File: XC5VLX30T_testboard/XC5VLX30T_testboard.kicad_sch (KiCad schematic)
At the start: 28 parts, among them J1 Conn_01x35_Pin, J10 Conn_01x04_Pin, J11 Conn_01x04_Pin, J12 Conn_01x04_Pin, J13 Conn_01x04_Pin, J14 Conn_01x04_Pin, J2 Conn_01x35_Pin, J3 Conn_01x35_Pin, J4 Conn_01x35_Pin, J5 Conn_01x35_Pin, J6 Conn_01x35_Pin, J7 Conn_01x35_Pin, J8 Conn_01x35_Pin, J9 Conn_01x04_Pin, U1 XC5VLX30T-1FFG665C, X1 SG-5032CCN

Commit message: mode select pins + pull down resistors
"If the Virtex-5 device is configured via JTAG on power-up, it is advisable to tie the mode pins to the Boundary-Scan configuration mode settings: 101 (M2 = 1, M1 = 0,
M0 = 1)."
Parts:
- added R1, R2, R3: R, Resistor_SMD:R_0201_0603Metric, symbol Device:R
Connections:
- net GND: now also R1.2
- net VCCO: now also R2.2, R3.2
- net M0_MODESELECT: now reaches U1.T20 (M0_0)
- net M0_MODESELECT: now also R3.1
- net M2_MODESELECT: now reaches U1.U20 (M2_0)
- net M2_MODESELECT: now also R2.1
- net M1_MODESELECT: now reaches U1.W20 (M1_0)
- net M1_MODESELECT: now also R1.1
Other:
- note removed: "top layer, 1st bottom row - AF"
- note removed: "top layer, 2nd bottom row - AE"

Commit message: resize wires to .13mm
resized wires to 0.13mm
added top layer gnd plane, vccaux plane
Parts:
- added C10, C11, C14, C16, C17: 470uF, Capacitor_Tantalum_SMD:CP_EIA-3216-12_Kemet-S, symbol Device:C
- added TP1, TP2, TP3, TP4: TestPoint, Connector_Pin:Pin_D0.7mm_L6.5mm_W1.8mm_FlatFork, symbol Connector:TestPoint
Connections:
- net GND: now also J10.3 (Pin_3), J10.4 (Pin_4), J11.1 (Pin_1), J11.2 (Pin_2), J12.3 (Pin_3), J12.4 (Pin_4), J13.1 (Pin_1), J13.2 (Pin_2), J14.3 (Pin_3), J14.4 (Pin_4), J9.1 (Pin_1), J9.2 (Pin_2), C10.2, C11.2, C14.2, C16.2, C17.2; no longer J10.1 (Pin_1), J10.2 (Pin_2), J11.3 (Pin_3), J11.4 (Pin_4), J12.1 (Pin_1), J12.2 (Pin_2), J13.3 (Pin_3), J13.4 (Pin_4), J14.1 (Pin_1), J14.2 (Pin_2), J9.3 (Pin_3), J9.4 (Pin_4)
- net IO_L8N_CC_SM1N_13: now also J6.30 (Pin_30); no longer J6.32 (Pin_32)
- net IO_L8P_CC_SM1P_13: now also J6.32 (Pin_32); no longer J6.31 (Pin_31)
- net IO_L9P_CC_SM0P_13: now also J6.31 (Pin_31); no longer J6.30 (Pin_30)
- net TCK: now also TP2.1
- net TDI: now also TP3.1
- net TDO: now also TP1.1
- net TMS: now also TP4.1
- net VCCO: now also J12.1 (Pin_1), J12.2 (Pin_2), C10.1, C11.1; no longer J12.3 (Pin_3), J12.4 (Pin_4)
- net VccAUX: now also J10.1 (Pin_1), J10.2 (Pin_2); no longer J10.3 (Pin_3), J10.4 (Pin_4)
- net VccINT: now also J14.1 (Pin_1), J14.2 (Pin_2); no longer J14.3 (Pin_3), J14.4 (Pin_4)
- net vccext: now also J11.3 (Pin_3), J11.4 (Pin_4), J13.3 (Pin_3), J13.4 (Pin_4), J9.3 (Pin_3), J9.4 (Pin_4), C14.1, C16.1, C17.1; no longer J11.1 (Pin_1), J11.2 (Pin_2), J13.1 (Pin_1), J13.2 (Pin_2), J9.1 (Pin_1), J9.2 (Pin_2)

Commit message: moved clock to P from N
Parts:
- added TP5: TestPoint, Connector_Pin:Pin_D0.7mm_L6.5mm_W1.8mm_FlatFork, symbol Connector:TestPoint
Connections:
- net CLK: now also U1.AC17 (IO_L8P_CC_GC_4); no longer U1.AC16 (IO_L9N_CC_GC_4)
- net GND: no longer J11.2 (Pin_2), J13.2 (Pin_2), J9.2 (Pin_2)
- net IO_L8P_CC_GC_4: now also U1.AC16 (IO_L9N_CC_GC_4); no longer U1.AC17 (IO_L8P_CC_GC_4)
- net vccext: no longer J11.3 (Pin_3), J13.3 (Pin_3), J9.3 (Pin_3)
- net CLK_AUX1: now reaches U1.D16 (IO_L1P_CC_GC_3)
- net CLK_AUX1: now also TP5.1
- no-connect marks 24 -> 188
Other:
- note added: "FPGA"
- note added: "VCCO capacitors"
- note added: "active crystal osc"
- note added: "jtag pins bottom side"
- note added: "power converters"
- note added: "vccaux capacitors"
- note added: "vccext capacitors"
- moved on the sheet: C1, C10, C11, C12, C13, C14, C15, C16, C17, C2, C3, C4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

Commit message: added jtag header and pi zero footprint
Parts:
- removed J10, J11, J12, J13, J14, J9: Conn_01x04_Pin, Connector_PinHeader_2.54mm:PinHeader_1x04_P2.54mm_Vertical, symbol Connector:Conn_01x04_Pin
- added J10: pi_zero_footprint_placeholder, pizero_23x58_mountholes:23x58pizero, symbol Connector_Generic:Conn_02x03_Counter_Clockwise
- added J11: Conn_01x02_Pin, Connector_PinSocket_2.54mm:PinSocket_1x02_P2.54mm_Vertical, symbol Connector:Conn_01x02_Pin
- added J15, J16, J17: Conn_01x06_Pin, virtex5_buck_footprint:virtex5_buck, symbol Connector:Conn_01x06_Pin
- added J9: Conn_02x03, Connector_PinHeader_2.54mm:PinHeader_2x03_P2.54mm_Vertical, symbol Connector_Generic:Conn_02x03_Counter_Clockwise
- added TP6, TP7, TP8, TP9: TestPoint, Connector_Pin:Pin_D0.7mm_L6.5mm_W1.8mm_FlatFork, symbol Connector:TestPoint
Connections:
- net GND: now also J11.1 (Pin_1), J15.3 (Pin_3), J15.4 (Pin_4), J15.5 (Pin_5), J16.3 (Pin_3), J16.4 (Pin_4), J16.5 (Pin_5), J17.3 (Pin_3), J17.4 (Pin_4), J17.5 (Pin_5), J9.2 (Pin_2)
- net VCCO: now also J17.1 (Pin_1), J17.2 (Pin_2), J9.1 (Pin_1)
- net VccAUX: now also J15.1 (Pin_1), J15.2 (Pin_2)
- net VccINT: now also J16.1 (Pin_1), J16.2 (Pin_2)
- net vccext: now also J11.2 (Pin_2), J15.6 (Pin_6), J16.6 (Pin_6), J17.6 (Pin_6)
- new net TCK_PAD: J9.5 (Pin_5), TP8.1
- new net TDI_PAD: J9.4 (Pin_4), TP7.1
- new net TDO_PAD: J9.6 (Pin_6), TP9.1
- new net TMS_PAD: J9.3 (Pin_3), TP6.1
- no-connect marks 188 -> 182
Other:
- moved on the sheet: TP1, TP2, TP3, TP4, TP5

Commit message: gnd planes
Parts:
- removed J10: pi_zero_footprint_placeholder, pizero_23x58_mountholes:23x58pizero, symbol Connector_Generic:Conn_02x03_Counter_Clockwise
- added J12: pi_zero_footprint_placeholder, pizero_23x58_mountholes:23x58pizero, symbol Connector_Generic:Conn_02x03_Counter_Clockwise
- TP1, TP2, TP3, TP4, TP5, TP6, TP7, TP8, TP9: footprint Connector_Pin:Pin_D0.7mm_L6.5mm_W1.8mm_FlatFork -> virtex5_buck_footprint:thisone_TestPoint_Pad_D1.0mm
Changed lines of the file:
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@@
 	(wire
 		(pts
+			(xy 60.96 469.9) (xy 69.85 469.9)
+		)
+		(stroke
+			(width 0)
+			(type default)
+		)
+	)
+	(wire
+		(pts
 			(xy 260.35 119.38) (xy 264.16 119.38)
 		)
@@
 	(wire
 		(pts
-			(xy 214.63 497.84) (xy 226.06 497.84)
-		)
-		(stroke
-			(width 0)
-			(type default)
-		)
-	)
-	(wire
-		(pts
 			(xy 861.06 85.09) (xy 857.25 85.09)
 		)
@@
 		)
 	)
+	(global_label "CLK_AUX1"
+		(shape input)
+		(at 69.85 469.9 0)
+		(fields_autoplaced yes)
+		(effects
+			(font
+				(size 1.27 1.27)
+			)
+			(justify left)
+		)
+		(property "Intersheetrefs" "${INTERSHEET_REFS}"
+			(at 82.209 469.9 0)
+			(effects
+				(font
+					(size 1.27 1.27)
+				)
+				(justify left)
+				(hide yes)
+			)
+		)
+	)
 	(global_label "IO_L18N_13"
 		(shape input)
@@
 		)
 	)
-	(global_label "CLK_AUX1"
-		(shape input)
-		(at 226.06 497.84 0)
-		(fields_autoplaced yes)
-		(effects
-			(font
-				(size 1.27 1.27)
-			)
-			(justify left)
-		)
-		(property "Intersheetrefs" "${INTERSHEET_REFS}"
-			(at 238.419 497.84 0)
-			(effects
-				(font
-					(size 1.27 1.27)
-				)
-				(justify left)
-				(hide yes)
-			)
-		)
-	)
 	(global_label "IO_L18N_18"
 		(shape bidirectional)
@@
 			)
 		)
-		(property "Footprint" "Connector_Pin:Pin_D0.7mm_L6.5mm_W1.8mm_FlatFork"
+		(property "Footprint" "virtex5_buck_footprint:thisone_TestPoint_Pad_D1.0mm"
 			(at 72.39 449.58 0)
 			(effects
@@
 			)
 		)
-		(property "Footprint" "Connector_Pin:Pin_D0.7mm_L6.5mm_W1.8mm_FlatFork"
+		(property "Footprint" "virtex5_buck_footprint:thisone_TestPoint_Pad_D1.0mm"
 			(at 132.08 443.23 0)
 			(effects
@@
 			)
 		)
-		(property "Footprint" "Connector_Pin:Pin_D0.7mm_L6.5mm_W1.8mm_FlatFork"
+		(property "Footprint" "virtex5_buck_footprint:thisone_TestPoint_Pad_D1.0mm"
 			(at 95.25 440.69 0)
 			(effects
@@
 	)
 	(symbol
+		(lib_id "Connector_Generic:Conn_02x03_Counter_Clockwise")
+		(at 469.9 596.9 0)
+		(unit 1)
+		(exclude_from_sim no)
+		(in_bom yes)
+		(on_board yes)
+		(dnp no)
+		(fields_autoplaced yes)
+		(property "Reference" "J12"
+			(at 471.17 588.01 0)
+			(effects
+				(font
+					(size 1.27 1.27)
+				)
+			)
+		)
+		(property "Value" "pi_zero_footprint_placeholder"
+			(at 471.17 590.55 0)
+			(effects
+				(font
+					(size 1.27 1.27)
+				)
+			)
+		)
+		(property "Footprint" "pizero_23x58_mountholes:23x58pizero"
+			(at 469.9 596.9 0)
+			(effects
+				(font
+					(size 1.27 1.27)
+				)
+				(hide yes)
+			)
+		)
+		(property "Datasheet" "~"
+			(at 469.9 596.9 0)
+			(effects
+				(font
+					(size 1.27 1.27)
+				)
+				(hide yes)
+			)
+		)
+		(property "Description" "Generic connector, double row, 02x03, counter clockwise pin numbering scheme (similar to DIP package numbering), script generated (kicad-library-utils/schlib/autogen/connector/)"
+			(at 469.9 596.9 0)
+			(effects
+				(font
+					(size 1.27 1.27)
+				)
+				(hide yes)
+			)
+		)
+		(pin "3"
+		)
+		(pin "2"
+		)
+		(pin "4"
+		)
+		(pin "5"
+		)
+		(pin "6"
+		)
+		(pin "1"
+		)
+		(instances
+			(project "XC5VLX30T_testboard"
+				(path "/67cccbfc-a73c-4a35-9756-6da624b7ab36"
+					(reference "J12")
+					(unit 1)
+				)
+			)
+		)
+	)
+	(symbol
 		(lib_id "power:GND")
 		(at 40.64 125.73 270)
@@
 			)
 		)
-		(property "Footprint" "Connector_Pin:Pin_D0.7mm_L6.5mm_W1.8mm_FlatFork"
+		(property "Footprint" "virtex5_buck_footprint:thisone_TestPoint_Pad_D1.0mm"
 			(at 129.54 439.42 0)
 			(effects
@@
 			)
 		)
-		(property "Footprint" "Connector_Pin:Pin_D0.7mm_L6.5mm_W1.8mm_FlatFork"
+		(property "Footprint" "virtex5_buck_footprint:thisone_TestPoint_Pad_D1.0mm"
 			(at 69.85 444.5 0)
 			(effects
@@
 	)
 	(symbol
+		(lib_id "Connector:TestPoint")
+		(at 60.96 469.9 0)
+		(unit 1)
+		(exclude_from_sim no)
+		(in_bom yes)
+		(on_board yes)
+		(dnp no)
+		(fields_autoplaced yes)
+		(property "Reference" "TP5"
+			(at 63.5 465.3279 0)
+			(effects
+				(font
+					(size 1.27 1.27)
+				)
+				(justify left)
+			)
+		)
+		(property "Value" "TestPoint"
+			(at 63.5 467.8679 0)
+			(effects
+				(font
+					(size 1.27 1.27)
+				)
+				(justify left)
+			)
+		)
+		(property "Footprint" "virtex5_buck_footprint:thisone_TestPoint_Pad_D1.0mm"
+			(at 66.04 469.9 0)
+			(effects
+				(font
+					(size 1.27 1.27)
+				)
+				(hide yes)
+			)
+		)
+		(property "Datasheet" "~"
+			(at 66.04 469.9 0)
+			(effects
+				(font
+					(size 1.27 1.27)
+				)
+				(hide yes)
+			)
+		)
+		(property "Description" "test point"
+			(at 60.96 469.9 0)
+			(effects
+				(font
+					(size 1.27 1.27)
+				)
+				(hide yes)
+			)
+		)
+		(pin "1"
+		)
+		(instances
+			(project "XC5VLX30T_testboard"
+				(path "/67cccbfc-a73c-4a35-9756-6da624b7ab36"
+					(reference "TP5")
+					(unit 1)
+				)
+			)
+		)
+	)
+	(symbol
 		(lib_id "power:GND")
 		(at 435.61 48.26 90)
@@
 	)
 	(symbol
-		(lib_id "Connector_Generic:Conn_02x03_Counter_Clockwise")
-		(at 443.23 600.71 0)
-		(unit 1)
-		(exclude_from_sim no)
-		(in_bom yes)
-		(on_board yes)
-		(dnp no)
-		(fields_autoplaced yes)
-		(property "Reference" "J10"
-			(at 444.5 591.82 0)
-			(effects
-				(font
-					(size 1.27 1.27)
-				)
-			)
-		)
-		(property "Value" "pi_zero_footprint_placeholder"
-			(at 444.5 594.36 0)
-			(effects
-				(font
-					(size 1.27 1.27)
-				)
-			)
-		)
-		(property "Footprint" "pizero_23x58_mountholes:23x58pizero"
-			(at 443.23 600.71 0)
-			(effects
-				(font
-					(size 1.27 1.27)
-				)
-				(hide yes)
-			)
-		)
-		(property "Datasheet" "~"
-			(at 443.23 600.71 0)
-			(effects
-				(font
-					(size 1.27 1.27)
-				)
-				(hide yes)
-			)
-		)
-		(property "Description" "Generic connector, double row, 02x03, counter clockwise pin numbering scheme (similar to DIP package numbering), script generated (kicad-library-utils/schlib/autogen/connector/)"
-			(at 443.23 600.71 0)
-			(effects
-				(font
-					(size 1.27 1.27)
-				)
-				(hide yes)
-			)
-		)
-		(pin "3"
-		)
-		(pin "2"
-		)
-		(pin "4"
-		)
-		(pin "5"
-		)
-		(pin "6"
-		)
-		(pin "1"
-		)
-		(instances
-			(project "XC5VLX30T_testboard"
-				(path "/67cccbfc-a73c-4a35-9756-6da624b7ab36"
-					(reference "J10")
-					(unit 1)
-				)
-			)
-		)
-	)
-	(symbol
 		(lib_id "power:GND")
 		(at 278.13 149.86 270)
@@
 	)
 	(symbol
-		(lib_id "Connector:TestPoint")
-		(at 214.63 497.84 0)
-		(unit 1)
-		(exclude_from_sim no)
-		(in_bom yes)
-		(on_board yes)
-		(dnp no)
-		(fields_autoplaced yes)
-		(property "Reference" "TP5"
-			(at 217.17 493.2679 0)
-			(effects
-				(font
-					(size 1.27 1.27)
-				)
-				(justify left)
-			)
-		)
-		(property "Value" "TestPoint"
-			(at 217.17 495.8079 0)
-			(effects
-				(font
-					(size 1.27 1.27)
-				)
-				(justify left)
-			)
-		)
-		(property "Footprint" "Connector_Pin:Pin_D0.7mm_L6.5mm_W1.8mm_FlatFork"
-			(at 219.71 497.84 0)
-			(effects
-				(font
-					(size 1.27 1.27)
-				)
-				(hide yes)
-			)
-		)
-		(property "Datasheet" "~"
-			(at 219.71 497.84 0)
-			(effects
-				(font
-					(size 1.27 1.27)
-				)
-				(hide yes)
-			)
-		)
-		(property "Description" "test point"
-			(at 214.63 497.84 0)
-			(effects
-				(font
-					(size 1.27 1.27)
-				)
-				(hide yes)
-			)
-		)
-		(pin "1"
-		)
-		(instances
-			(project "XC5VLX30T_testboard"
-				(path "/67cccbfc-a73c-4a35-9756-6da624b7ab36"
-					(reference "TP5")
-					(unit 1)
-				)
-			)
-		)
-	)
-	(symbol
 		(lib_id "power:GND")
 		(at 176.53 271.78 90)
@@
 			)
 		)
-		(property "Footprint" "Connector_Pin:Pin_D0.7mm_L6.5mm_W1.8mm_FlatFork"
+		(property "Footprint" "virtex5_buck_footprint:thisone_TestPoint_Pad_D1.0mm"
 			(at 67.31 439.42 0)
 			(effects
@@
 			)
 		)
-		(property "Footprint" "Connector_Pin:Pin_D0.7mm_L6.5mm_W1.8mm_FlatFork"
+		(property "Footprint" "virtex5_buck_footprint:thisone_TestPoint_Pad_D1.0mm"
 			(at 76.2 455.93 0)
 			(effects
@@
 			)
 		)
-		(property "Footprint" "Connector_Pin:Pin_D0.7mm_L6.5mm_W1.8mm_FlatFork"
+		(property "Footprint" "virtex5_buck_footprint:thisone_TestPoint_Pad_D1.0mm"
 			(at 127 450.85 0)
 			(effects

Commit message: removed 4 i/o for wider vccint
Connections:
- net GND: now also J12.1 (Pin_1), J4.10 (Pin_10), J4.11 (Pin_11), J4.8 (Pin_8), J4.9 (Pin_9)
- net IO_L0P_SM8P_13: now also J6.10 (Pin_10); no longer J6.11 (Pin_11)
- net IO_L10P_CC_12: now also J1.13 (Pin_13); no longer J1.15 (Pin_15)
- net IO_L11P_CC_12: now also J1.29 (Pin_29); no longer J1.27 (Pin_27)
- net IO_L12N_VRP_15: now also J4.32 (Pin_32); no longer J4.33 (Pin_33)
- net IO_L12P_VRN_17: now also J7.5 (Pin_5); no longer J7.6 (Pin_6)
- net IO_L13N_17: now also J7.3 (Pin_3); no longer J7.4 (Pin_4)
- net IO_L13P_12: now also J1.27 (Pin_27); no longer J1.29 (Pin_29)
- net IO_L13P_17: now also J7.6 (Pin_6); no longer J7.5 (Pin_5)
- net IO_L14N_VREF_15: now also J4.33 (Pin_33); no longer J4.32 (Pin_32)
- net IO_L16P_SM12P_11: now also J6.8 (Pin_8); no longer J6.9 (Pin_9)
- net IO_L18N_SM10N_11: now also J6.11 (Pin_11); no longer J6.10 (Pin_10)
- net IO_L19N_SM9N_11: now also J6.9 (Pin_9); no longer J6.8 (Pin_8)
- net IO_L7P_12: now also J1.15 (Pin_15); no longer J1.13 (Pin_13)
- net IO_L9P_CC_17: now also J7.4 (Pin_4); no longer J7.3 (Pin_3)
- net IO_L0N_15: no longer names the net of U1.C14 (IO_L0N_15)
- net IO_L0N_15: no longer J4.9 (Pin_9)
- net IO_L0P_15: no longer names the net of U1.C13 (IO_L0P_15)
- net IO_L0P_15: no longer J4.8 (Pin_8)
- net IO_L1P_15: no longer names the net of U1.B14 (IO_L1P_15)
- net IO_L1P_15: no longer J4.11 (Pin_11)
- net IO_L2P_15: no longer names the net of U1.A14 (IO_L2P_15)
- net IO_L2P_15: no longer J4.10 (Pin_10)
- no-connect marks 182 -> 186

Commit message: w
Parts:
- X1: footprint Crystal:Crystal_SMD_3225-4Pin_3.2x2.5mm_HandSoldering -> Crystal:Crystal_SMD_7050-4Pin_7.0x5.0mm
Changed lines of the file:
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@@
 			)
 		)
-		(property "Footprint" "Crystal:Crystal_SMD_3225-4Pin_3.2x2.5mm_HandSoldering"
+		(property "Footprint" "Crystal:Crystal_SMD_7050-4Pin_7.0x5.0mm"
 			(at 88.9 525.78 0)
 			(effects
@@
 		)
 		(instances
-			(project ""
+			(project "XC5VLX30T_testboard"
 				(path "/67cccbfc-a73c-4a35-9756-6da624b7ab36"
 					(reference "J15")
@@
 		)
 		(instances
-			(project ""
+			(project "XC5VLX30T_testboard"
 				(path "/67cccbfc-a73c-4a35-9756-6da624b7ab36"
 					(reference "J9")
@@
 		)
 		(instances
-			(project ""
+			(project "XC5VLX30T_testboard"
 				(path "/67cccbfc-a73c-4a35-9756-6da624b7ab36"
 					(reference "J11")
@@
 		)
 		(instances
-			(project ""
+			(project "XC5VLX30T_testboard"
 				(path "/67cccbfc-a73c-4a35-9756-6da624b7ab36"
 					(reference "TP1")

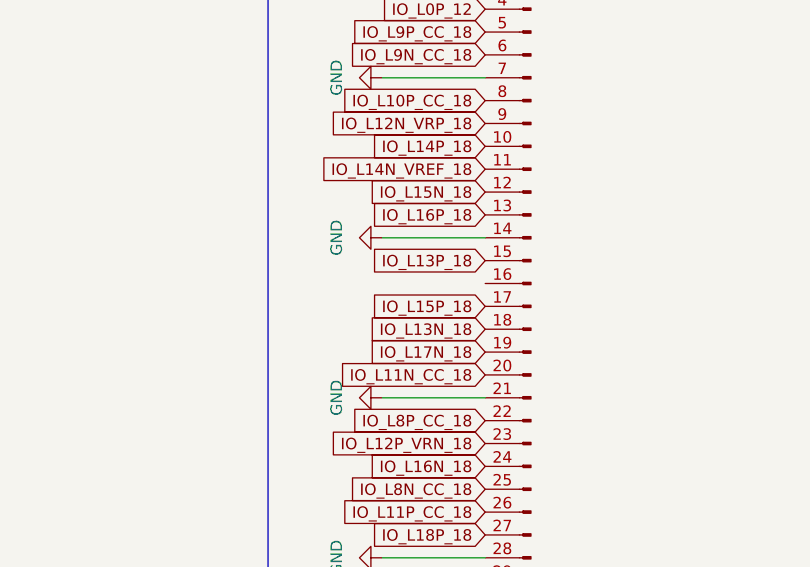
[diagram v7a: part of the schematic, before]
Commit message: centered holes
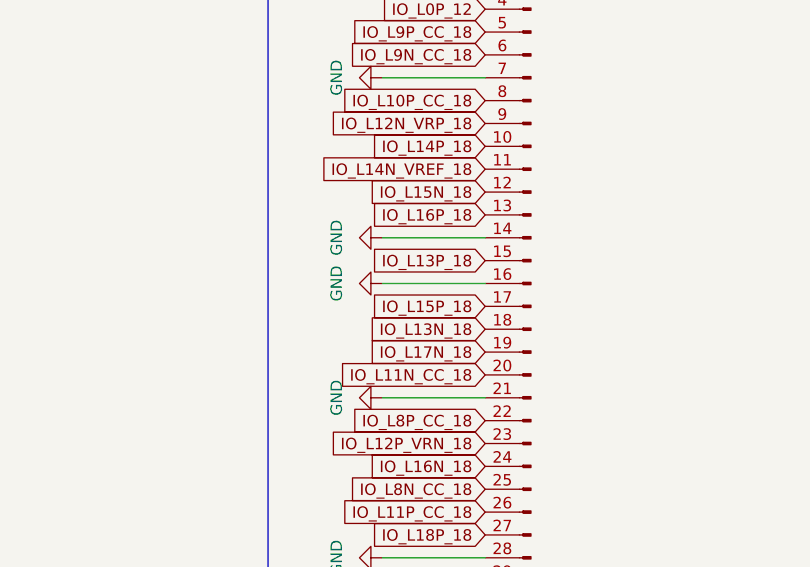
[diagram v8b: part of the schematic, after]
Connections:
- net GND: now also J2.16 (Pin_16)
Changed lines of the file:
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@@
 	(wire
 		(pts
+			(xy 375.92 579.12) (xy 387.35 579.12)
+		)
+		(stroke
+			(width 0)
+			(type default)
+		)
+	)
+	(wire
+		(pts
 			(xy 698.5 262.89) (xy 702.31 262.89)
 		)
@@
 					(unit 1)
 				)
+			)
+		)
+	)
+	(symbol
+		(lib_id "power:GND")
+		(at 375.92 579.12 270)
+		(unit 1)
+		(exclude_from_sim no)
+		(in_bom yes)
+		(on_board yes)
+		(dnp no)
+		(fields_autoplaced yes)
+		(property "Reference" "#PWR0242"
+			(at 369.57 579.12 0)
+			(effects
+				(font
+					(size 1.27 1.27)
+				)
+				(hide yes)
+			)
+		)
+		(property "Value" "GND"
+			(at 370.84 579.12 0)
+			(effects
+				(font
+					(size 1.27 1.27)
+				)
+			)
+		)
+		(property "Footprint" ""
+			(at 375.92 579.12 0)
+			(effects
+				(font
+					(size 1.27 1.27)
+				)
+				(hide yes)
+			)
+		)
+		(property "Datasheet" ""
+			(at 375.92 579.12 0)
+			(effects
+				(font
+					(size 1.27 1.27)
+				)
+				(hide yes)
+			)
+		)
+		(property "Description" "Power symbol creates a global label with name \"GND\" , ground"
+			(at 375.92 579.12 0)
+			(effects
+				(font
+					(size 1.27 1.27)
+				)
+				(hide yes)
+			)
+		)
+		(pin "1"
+		)
+		(instances
+			(project "XC5VLX30T_testboard"
+				(path "/67cccbfc-a73c-4a35-9756-6da624b7ab36"
+					(reference "#PWR0242")
+					(unit 1)
+				)
